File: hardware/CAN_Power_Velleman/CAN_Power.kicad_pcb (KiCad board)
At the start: 2 copper layers, 19 parts, among them K1 CONN_3, K2 CONN_3, P1 CONN_1, P2 CONN_1, P3 CONN_1, P5 CONN_4, P6 CONN_1, P7 CONN_1, P8 CONN_1, P9 FUSE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

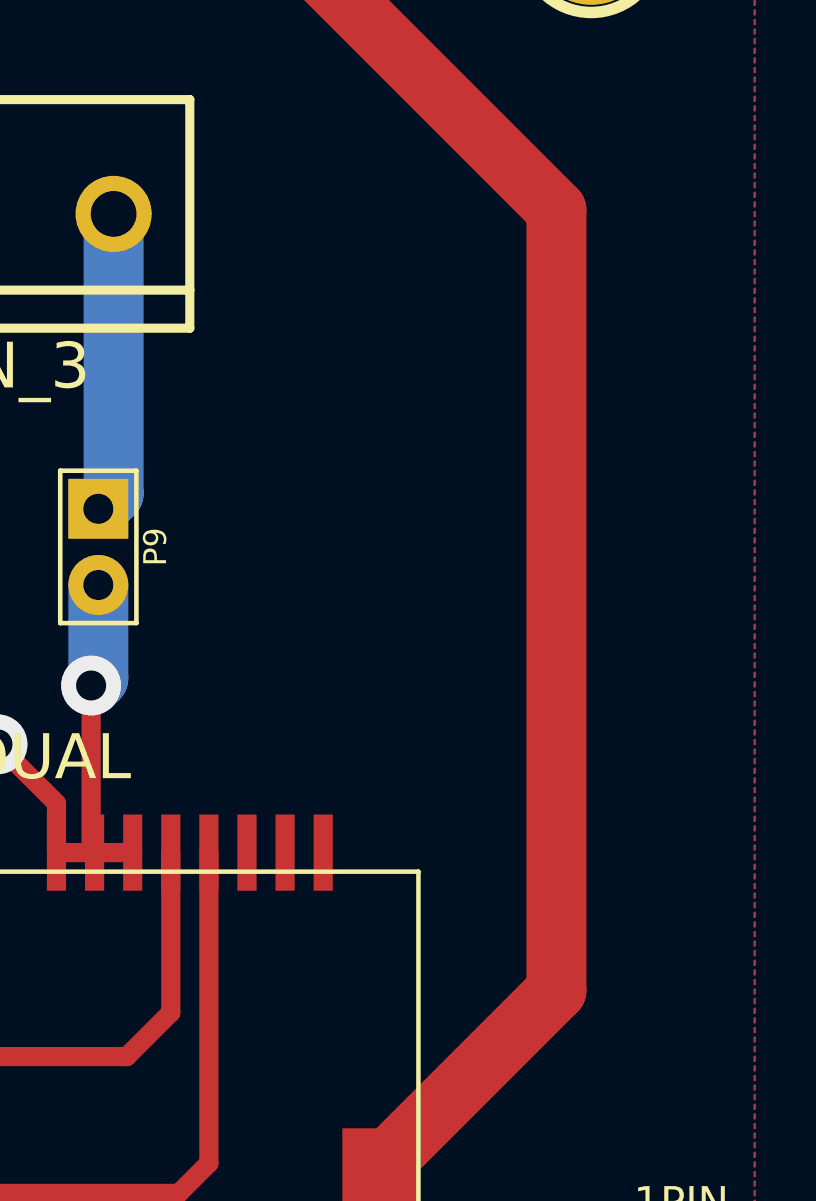
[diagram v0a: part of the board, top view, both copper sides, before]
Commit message: Connected PE to GND
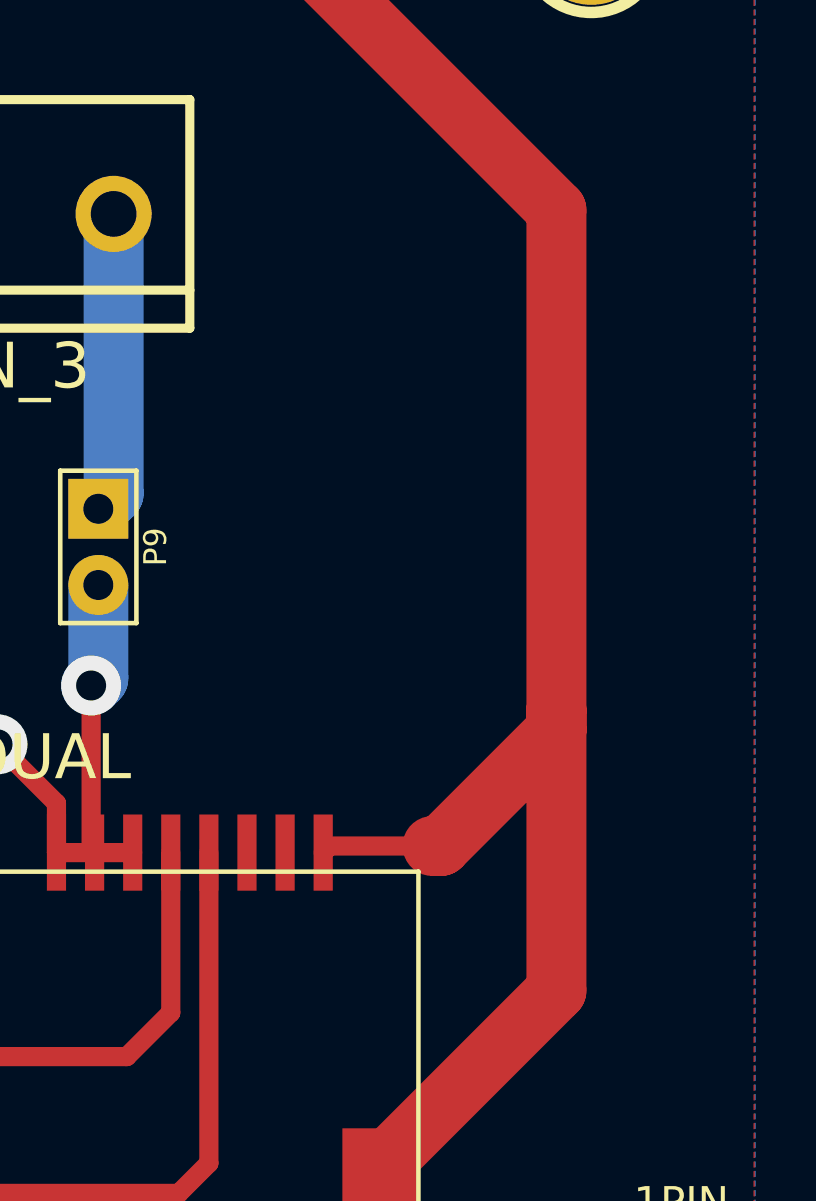
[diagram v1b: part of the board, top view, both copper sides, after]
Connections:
- K2 pad 1: GNDPWR -> GND
- U1 pad 17: GNDPWR -> GND
- U1 pad 18: GNDPWR -> GND
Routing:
- net GND: track 23.1 -> 302.0 mm, vias 1 -> 3
- net GNDPWR: track 268.6 -> 0.00 mm, vias 2 -> 0
